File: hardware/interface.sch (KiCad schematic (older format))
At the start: 75 parts, among them J46 Conn_01x03, J47 Conn_01x03, J60 USB_C_Receptacle, J61 Micro_SD_Card_Det, J62 Conn_01x02, J63 Conn_01x02, J66 Conn_01x03, J67 Conn_01x03, J71 Conn_01x02, J72 Conn_01x02, J73 Conn_01x02, J74 Conn_01x02, Q2 AO3401, U5 MAX6675, U6 MAX6675

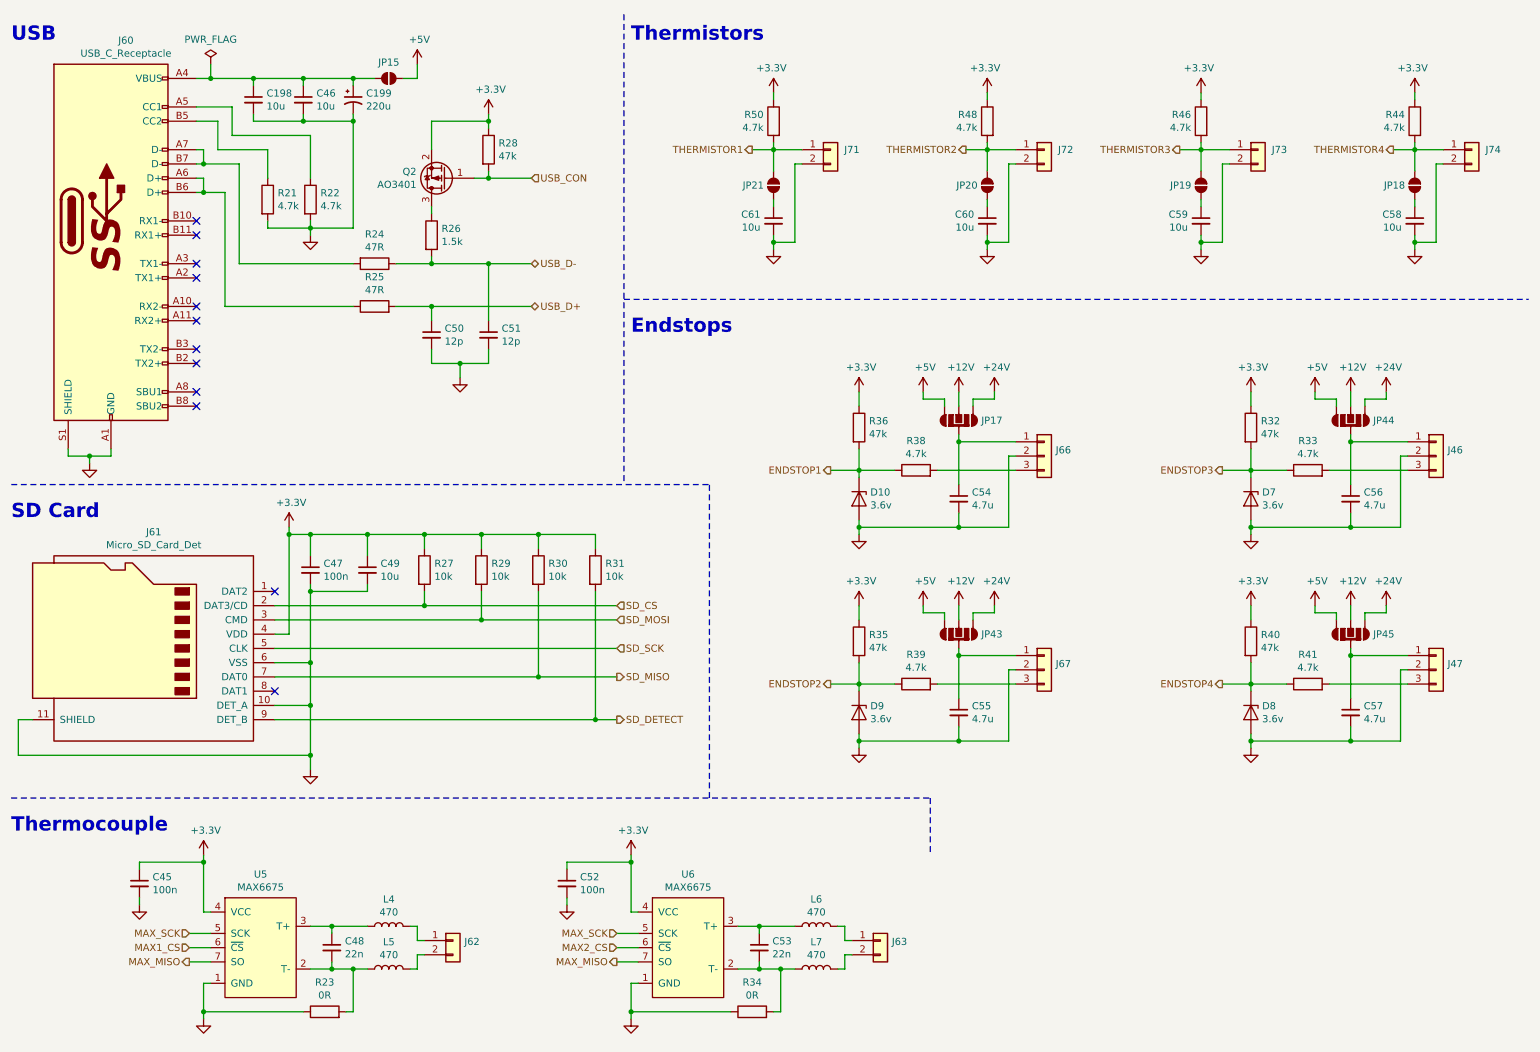
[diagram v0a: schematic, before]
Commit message: replaced stepper driver
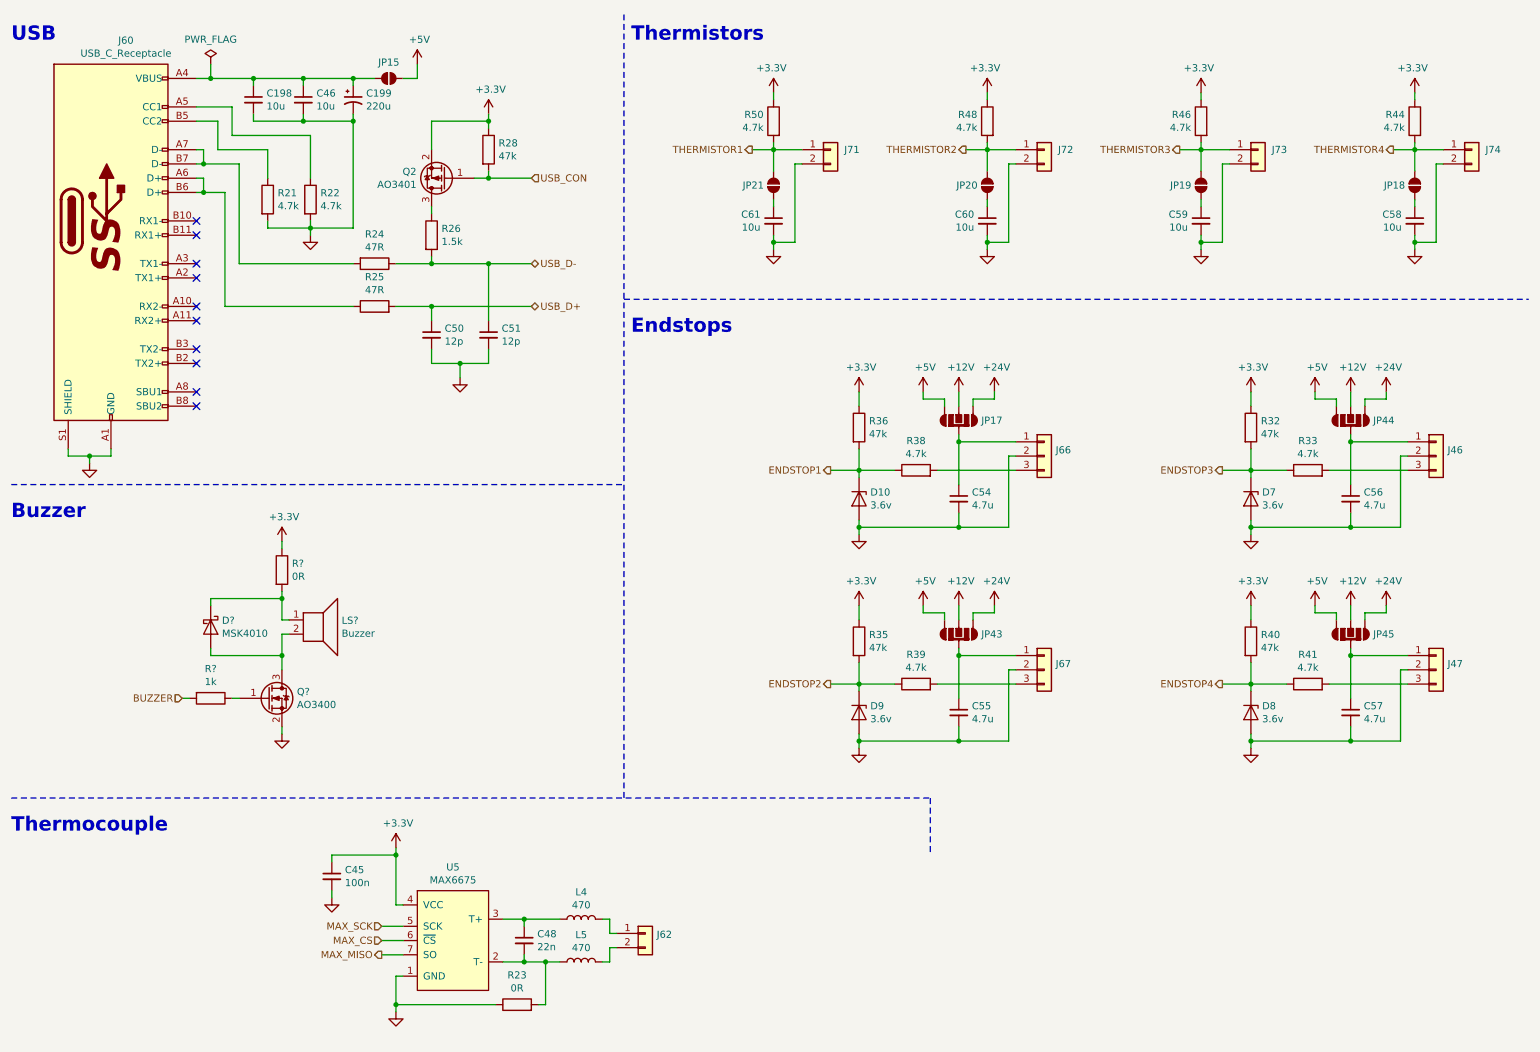
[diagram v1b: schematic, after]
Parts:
- removed C47, C52: 100n, _Generic:0603_CAP, symbol Device:C_Small
- removed C49: 10u, _Generic:0603_CAP, symbol Device:C_Small
- removed C53: 22n, _Generic:0603_CAP, symbol Device:C_Small
- removed J61: Micro_SD_Card_Det, _Generic:HYC77-TF09-200, symbol Connector:Micro_SD_Card_Det
- removed J63: Conn_01x02, _Generic:JST_XH_2P, symbol Connector_Generic:Conn_01x02
- removed L6, L7: 470, _Generic:0603_IND, symbol Device:L
- removed R27, R29, R30, R31: 10k, _Generic:0603_RES, symbol Device:R
- removed R34: 0R, _Generic:0603_RES, symbol Device:R
- removed U6: MAX6675, _Generic:SO-8, symbol #Sensor:MAX6675
- added D?: MSK4010, _Generic:SOD-523_DIODE, symbol Device:D_Schottky
- added LS?: Buzzer, _Generic:Buzzer-7525, symbol Device:Speaker
- added Q?: AO3400, _Generic:SOT-23, symbol Device:Q_NMOS_GSD
- added R?: 0R, _Generic:0603_RES, symbol Device:R
- added R?: 1k, _Generic:0603_RES, symbol Device:R
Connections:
- net +3V3: now also R?.1
- net GND: now also Q?.2 (S)
- net MAX1_CS renamed MAX_CS
- new net: D?.1 (K), LS?.1, R?.2
- new net: D?.2 (A), LS?.2, Q?.3 (D)
- new net: Q?.1 (G), R?.1
- new net BUZZER: R?.2
- no-connect marks 12 -> 10
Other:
- note added: "Buzzer"
- note removed: "SD Card"
- moved on the sheet: C45, C48, J62, L4, L5, R23, U5

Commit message: layout
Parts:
- removed C199: 220u, Capacitor_SMD:CP_Elec_6.3x7.7, symbol Device:CP1_Small
- removed C46: 10u, _Generic:0603_CAP, symbol Device:C_Small
- removed C50, C51: 12p, _Generic:0603_CAP, symbol Device:C_Small
- removed Q2: AO3401, _Generic:SOT-23, symbol Device:Q_PMOS_GSD
- removed R24, R25: 47R, _Generic:0603_RES, symbol Device:R
- removed R26: 1.5k, _Generic:0603_RES, symbol Device:R
- removed R28: 47k, _Generic:0603_RES, symbol Device:R
- removed R?: 0R, _Generic:0603_RES, symbol Device:R
- added FB1: Ferrite_Bead_Small, _Generic:0805_IND, symbol Device:Ferrite_Bead_Small
- added JP1: SolderJumper_2_Open, _Generic:Solder Jumper 2P, symbol #PCB_Only:SolderJumper_2_Open
- gave numbers to parts that had none: 4
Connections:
- net +3V3: now also D2.1 (K), LS1.1
- net BUZZER: now also JP1.1 (A); no longer R16.2
- net GND: now also FB1.1; no longer J60.S1 (SHIELD)
- net USB_D+: now also J60.A6 (D+), J60.B6 (D+)
- net USB_D-: now also J60.A7 (D-), J60.B7 (D-)
- new net: FB1.2, J60.S1 (SHIELD)
- new net: JP1.2 (B), R16.2
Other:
- moved on the sheet: C198, C45, C48, C54, C55, C56, C57, C58, C59, C60, C61, D10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

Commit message: layout
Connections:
- net +24V: now also JP43.2 (O1), JP44.2 (O1); no longer JP43.4 (O4), JP44.4 (O4)
- net +5V: now also JP43.4 (O4), JP44.4 (O4); no longer JP43.2 (O1), JP44.2 (O1)
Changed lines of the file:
@@
 F 3 "~" H 5100 1250 50  0001 C CNN
 	1    5100 1250
-	1    0    0    -1
+	-1   0    0    -1
 $EndComp
 $Comp
@@
 F 3 "~" H 7600 1250 50  0001 C CNN
 	1    7600 1250
-	1    0    0    -1
+	-1   0    0    -1
 $EndComp
 $Comp

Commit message: combine
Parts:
- removed C54, C55, C56, C57: 4.7u, _Generic:0805_CAP, symbol Device:C_Small
- removed C58: 10u, _Generic:0603_CAP, symbol Device:C_Small
- removed D10, D7, D8, D9: 3.6v, _Generic:SOD-523_DIODE, symbol Device:D_Zener
- removed J46, J47, J66, J67: Conn_01x03, _Generic:JST_XH_3P, symbol Connector_Generic:Conn_01x03
- removed J74: Conn_01x02, _Generic:JST_XH_2P, symbol Connector_Generic:Conn_01x02
- removed JP17, JP43, JP44, JP45: SolderJumper_4_Open, _Generic:SolderJumper_JST, symbol #PCB_Only:SolderJumper_4_Open
- removed JP18, JP19, JP20, JP21: SolderJumper_2_Open, _Generic:Solder Jumper 2P, symbol #PCB_Only:SolderJumper_2_Open
- removed R32, R35, R36, R40: 47k, _Generic:0603_RES, symbol Device:R
- removed R33, R38, R39, R41, R44: 4.7k, _Generic:0603_RES, symbol Device:R
- added C?: 100n, _Generic:0603_CAP, symbol Device:C_Small
- added C?: 10u, _Generic:0603_CAP, symbol Device:C_Small
- added C? (x2): 220u, Capacitor_SMD:CP_Elec_6.3x7.7, symbol Device:CP1_Small
- added C? (x8): 4.7u, _Generic:1210_CAP, symbol Device:C_Small
- added D? (x2): LED, _Generic:0603_LED, symbol Device:LED_Small
- added F? (x2): Fuse, _Generic:1206_RES, symbol Device:Fuse
- added J?: Screw_Terminal_01x04, _Generic:KF635-4P, symbol Connector:Screw_Terminal_01x04
- added Q? (x2): AON7418, _Generic:DFN3x3A_8L_EP1_P, symbol Device:Q_NMOS_SGD
- added R? (x2): 10R, _Generic:0603_RES, symbol Device:R
- added R? (x2): 1k, _Generic:0603_RES, symbol Device:R
- added U?: IR4427S, _Generic:SO-8, symbol Driver_FET:MIC4427
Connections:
- net +12V: now also C?.1, C?.1, R?.1, R?.1, U?.6 (V+)
- net +24V: now also C?.1, C?.1, F?.2, F?.2
- net GND: now also C?.2, C?.2, U?.3 (GND)
- net THERMISTOR1: now also C61.1
- net THERMISTOR2: now also C60.1
- net THERMISTOR3: now also C59.1
- new net: D?.1 (K), J?.1 (Pin_1), Q?.3 (D)
- new net: C?.1, C?.1, C?.1, C?.1, F?.1, J?.2 (Pin_2)
- new net: D?.1 (K), J?.3 (Pin_3), Q?.3 (D)
- new net: C?.1, C?.1, C?.1, C?.1, F?.1, J?.4 (Pin_4)
- new net: Q?.2 (G), R?.1 (x2)
- new net: R?.2, U?.5 (OUT_B)
- new net: R?.2, U?.7 (OUT_A)
- new net: D?.2 (A), R?.2 (x2)
- new net DCIN-: C?.2, C?.2, C?.2, C?.2, C?.2, C?.2, C?.2, C?.2, C?.2, C?.2, Q?.1 (S), Q?.1 (S)
- new net POWER_OUT1: U?.2 (IN_A)
- new net POWER_OUT2: U?.4 (IN_B)
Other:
- note added: "High Power Outputs"
- note removed: "Endstops"
- moved on the sheet: C59, C60, C61, J71, J72, J73, R46, R48, R50
